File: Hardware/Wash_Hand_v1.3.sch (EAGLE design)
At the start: 59 parts, among them IC1 LM358D, IC2 LP298XS, IC3 4050D, J1 I2C, J2 ICSP, J3 SPI, J5 EXT_VCC, J6 6_PIN_SERIAL_CABLEPTH, Q1 16.0 Mhz, U1 328P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

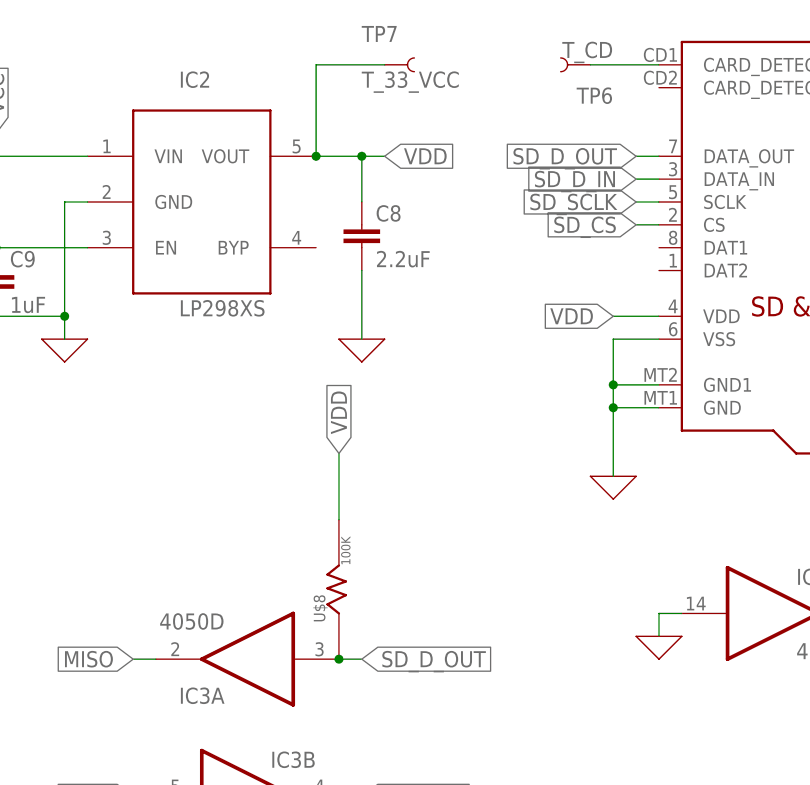
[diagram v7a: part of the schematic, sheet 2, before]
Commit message: Board/Schematic: Add 0.01uF bypass to LP2985
Signed-off-by: Konrad Rzeszutek Wilk <konrad@kernel.org>
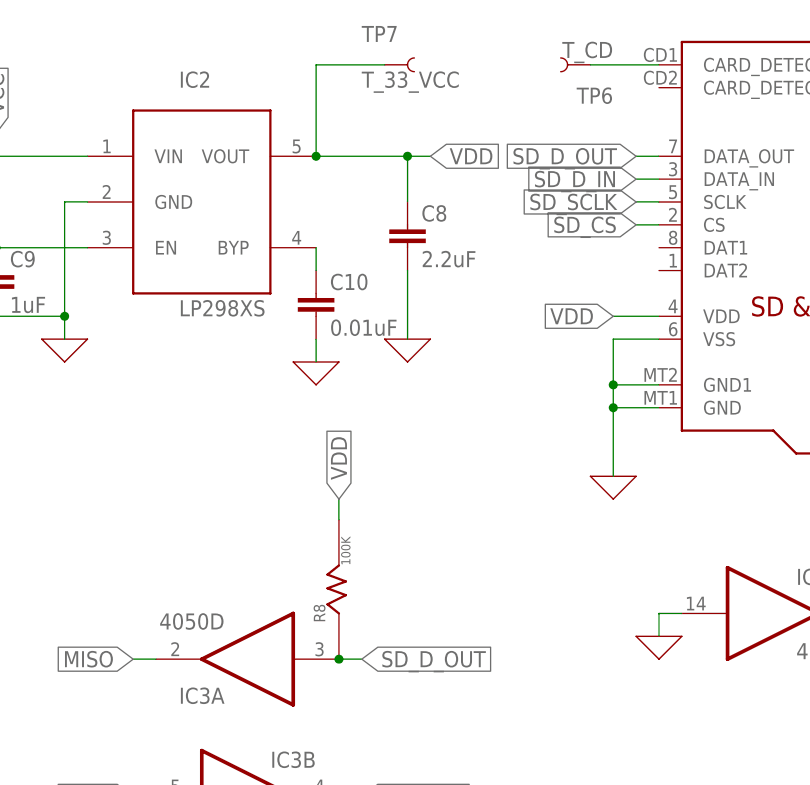
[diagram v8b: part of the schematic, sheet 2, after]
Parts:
- added C10: 0.01uF, SparkFun-Capacitors:1.0UF-1206-50V-10%
- renumbered U$8 to R8
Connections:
- new net N$13: C10.1, IC2.BYP
- net 0: now also C10.2
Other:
- moved on the sheet: C8
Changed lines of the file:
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@@
 <part name="C9" library="SparkFun-Capacitors" library_urn="urn:adsk.eagle:library:510" deviceset="1.0UF" device="-1206-50V-10%" package3d_urn="urn:adsk.eagle:package:37426/1" value="1uF"/>
 <part name="X_24" library="ngspice-simulation" library_urn="urn:adsk.eagle:library:527439" deviceset="GND" device=""/>
-<part name="U$8" library="darnok_common" deviceset="RESISTOR" device="R1206" value="100K"/>
+<part name="R8" library="darnok_common" deviceset="RESISTOR" device="R1206" value="100K"/>
+<part name="C10" library="SparkFun-Capacitors" library_urn="urn:adsk.eagle:library:510" deviceset="1.0UF" device="-1206-50V-10%" package3d_urn="urn:adsk.eagle:package:37426/1" value="0.01uF"/>
+<part name="X_25" library="ngspice-simulation" library_urn="urn:adsk.eagle:library:527439" deviceset="GND" device=""/>
 </parts>
 <sheets>
@@
 <instance part="X_22" gate="G$1" x="93.98" y="66.04" smashed="yes"/>
 <instance part="X_23" gate="G$1" x="111.76" y="73.66" smashed="yes"/>
-<instance part="C8" gate="G$1" x="48.26" y="152.4" smashed="yes">
-<attribute name="NAME" x="49.784" y="155.321" size="1.778" layer="95" font="vector"/>
-<attribute name="VALUE" x="49.784" y="150.241" size="1.778" layer="96" font="vector"/>
+<instance part="C8" gate="G$1" x="53.34" y="152.4" smashed="yes">
+<attribute name="NAME" x="54.864" y="155.321" size="1.778" layer="95" font="vector"/>
+<attribute name="VALUE" x="54.864" y="150.241" size="1.778" layer="96" font="vector"/>
 </instance>
 <instance part="C9" gate="G$1" x="7.62" y="147.32" smashed="yes">
@@
 <attribute name="VALUE" x="9.144" y="145.161" size="1.778" layer="96" font="vector"/>
 </instance>
-<instance part="X_24" gate="G$1" x="48.26" y="142.24" smashed="yes"/>
-<instance part="U$8" gate="G$1" x="45.72" y="111.76" smashed="yes" rot="R90">
+<instance part="X_24" gate="G$1" x="53.34" y="142.24" smashed="yes"/>
+<instance part="R8" gate="G$1" x="45.72" y="111.76" smashed="yes" rot="R90">
 <attribute name="NAME" x="44.196" y="110.744" size="1.27" layer="95" rot="R90"/>
 <attribute name="VALUE" x="46.99" y="117.094" size="1.016" layer="96" rot="R90"/>
 </instance>
+<instance part="C10" gate="G$1" x="43.18" y="144.78" smashed="yes">
+<attribute name="NAME" x="44.704" y="147.701" size="1.778" layer="95" font="vector"/>
+<attribute name="VALUE" x="44.704" y="142.621" size="1.778" layer="96" font="vector"/>
+</instance>
+<instance part="X_25" gate="G$1" x="43.18" y="139.7" smashed="yes"/>
 </instances>
 <busses>
@@
 <segment>
 <pinref part="C8" gate="G$1" pin="2"/>
-<wire x1="48.26" y1="149.86" x2="48.26" y2="142.24" width="0.1524" layer="91"/>
+<wire x1="53.34" y1="149.86" x2="53.34" y2="142.24" width="0.1524" layer="91"/>
 <pinref part="X_24" gate="G$1" pin="0"/>
+</segment>
+<segment>
+<pinref part="C10" gate="G$1" pin="2"/>
+<wire x1="43.18" y1="142.24" x2="43.18" y2="139.7" width="0.1524" layer="91"/>
+<pinref part="X_25" gate="G$1" pin="0"/>
 </segment>
 </net>
@@
 <wire x1="45.72" y1="106.68" x2="48.26" y2="106.68" width="0.1524" layer="91"/>
 <label x="48.26" y="106.68" size="1.778" layer="95" xref="yes"/>
-<pinref part="U$8" gate="G$1" pin="R_1"/>
+<pinref part="R8" gate="G$1" pin="R_1"/>
 <junction x="45.72" y="106.68"/>
 </segment>
@@
 <segment>
 <pinref part="IC2" gate="G$1" pin="VOUT"/>
-<wire x1="43.18" y1="162.56" x2="48.26" y2="162.56" width="0.1524" layer="91"/>
-<label x="50.8" y="162.56" size="1.778" layer="95" xref="yes"/>
-<wire x1="48.26" y1="162.56" x2="50.8" y2="162.56" width="0.1524" layer="91"/>
+<wire x1="43.18" y1="162.56" x2="53.34" y2="162.56" width="0.1524" layer="91"/>
+<label x="55.88" y="162.56" size="1.778" layer="95" xref="yes"/>
+<wire x1="53.34" y1="162.56" x2="55.88" y2="162.56" width="0.1524" layer="91"/>
 <wire x1="43.18" y1="162.56" x2="43.18" y2="172.72" width="0.1524" layer="91"/>
 <junction x="43.18" y="162.56"/>
@@
 <wire x1="43.18" y1="172.72" x2="50.8" y2="172.72" width="0.1524" layer="91"/>
 <pinref part="C8" gate="G$1" pin="1"/>
-<wire x1="48.26" y1="157.48" x2="48.26" y2="162.56" width="0.1524" layer="91"/>
-<junction x="48.26" y="162.56"/>
+<wire x1="53.34" y1="157.48" x2="53.34" y2="162.56" width="0.1524" layer="91"/>
+<junction x="53.34" y="162.56"/>
 </segment>
 <segment>
@@
 </segment>
 <segment>
-<pinref part="U$8" gate="G$1" pin="R_2"/>
-<wire x1="45.72" y1="122.174" x2="45.72" y2="129.54" width="0.1524" layer="91"/>
-<label x="45.72" y="129.54" size="1.778" layer="95" rot="R90" xref="yes"/>
+<pinref part="R8" gate="G$1" pin="R_2"/>
+<wire x1="45.72" y1="122.174" x2="45.72" y2="124.46" width="0.1524" layer="91"/>
+<label x="45.72" y="124.46" size="1.778" layer="95" rot="R90" xref="yes"/>
 </segment>
 </net>
@@
 </segment>
 </net>
+<net name="N$13" class="0">
+<segment>
+<pinref part="IC2" gate="G$1" pin="BYP"/>
+<wire x1="43.18" y1="152.4" x2="43.18" y2="149.86" width="0.1524" layer="91"/>
+<pinref part="C10" gate="G$1" pin="1"/>
+</segment>
+</net>
